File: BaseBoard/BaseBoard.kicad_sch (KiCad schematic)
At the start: 29 parts, among them J1 IMU, J2 Conn_01x04, J3 Raspberry_Pi_2_3, J4 USB_C_Receptacle_USB2.0, J5 Conn_02x04, SW1 SW_Push, SW2 SW_Push, U1 GD32VF103Cx, Y1 8Mhz

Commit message: 使用功率地
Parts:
- removed U1: GD32VF103Cx, Package_QFP:LQFP-48_7x7mm_P0.5mm, symbol GD32VF103:GD32VF103Cx
- added JP1: SolderJumper_2_Bridged, Jumper:SolderJumper-2_P1.3mm_Bridged2Bar_Pad1.0x1.5mm, symbol Jumper:SolderJumper_2_Bridged
- added U1: GD32VF103C8Tx, Package_QFP:LQFP-48_7x7mm_P0.5mm, symbol MCU_ST_STM32F1:STM32F103C8Tx
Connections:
- net +3V3: now also SW1.1, U1.1 (VBAT), U1.24 (VDD), U1.36 (VDD), U1.48 (VDD), U1.9 (VDDA); no longer SW1.2
- net ADC: now also U1.18 (PB0)
- net BOOT0: now also SW1.2, U1.44 (BOOT0); no longer SW1.1
- net BOOT1: now also U1.20 (PB2)
- net CTL_RX: now also U1.13 (PA3)
- net CTL_TX: now also U1.12 (PA2)
- net DEBUG_RX: now also U1.22 (PB11)
- net DEBUG_TX: now also U1.21 (PB10)
- net ENC1_A: now also U1.40 (PB4)
- net ENC1_B: now also U1.41 (PB5)
- net ENC2_A: now also U1.42 (PB6)
- net ENC2_B: now also U1.43 (PB7)
- net ENC3_A: now also U1.10 (PA0)
- net ENC3_B: now also U1.11 (PA1)
- net GND: now also JP1.1 (A), U1.23 (VSS), U1.35 (VSS), U1.47 (VSS), U1.8 (VSSA)
- net JTCK: now also U1.37 (PA14)
- net JTDI: now also U1.38 (PA15)
- net JTDO: now also U1.39 (PB3)
- net JTMS: now also U1.34 (PA13)
- net OSC32_IN: now also U1.3 (PC14)
- net OSC32_OUT: now also U1.4 (PC15)
- net OSCIN: now also U1.5 (PD0)
- net OSCOUT: now also U1.6 (PD1)
- net PWM1: now also U1.29 (PA8)
- net PWM1_ON: now also U1.26 (PB13)
- net PWM2: now also U1.30 (PA9)
- net PWM2_ON: now also U1.27 (PB14)
- net PWM3: now also U1.31 (PA10)
- net PWM3_ON: now also U1.28 (PB15)
- net USB_DM: now also U1.32 (PA11)
- net USB_DP: now also U1.33 (PA12)
- net at D1.1 (K): now also U1.2 (PC13)
- net at C8.1, R7.1, SW2.2: now also U1.7 (NRST)
- new net GNDPWR: JP1.2 (B)
- no-connect marks 6 -> 2
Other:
- moved on the sheet: C8, D1, R7, R8, SW2

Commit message: 临时提交
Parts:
- added J13: Conn_01x02_Female, Connector_JST:JST_PH_S2B-PH-K_1x02_P2.00mm_Horizontal, symbol Connector:Conn_01x02_Female
- added J14: Conn_01x03_Female, Connector_JST:JST_PH_S3B-PH-K_1x03_P2.00mm_Horizontal, symbol Connector:Conn_01x03_Female
- added R11: 10k, Resistor_SMD:R_0805_2012Metric, symbol Device:R_Small
- J2: footprint Connector_JST:JST_XH_B4B-XH-A_1x04_P2.50mm_Vertical -> Connector_JST:JST_PH_S4B-PH-K_1x04_P2.00mm_Horizontal
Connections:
- net +3V3: now also SW1.2, R11.1; no longer SW1.1
- net BOOT0: now also SW1.1; no longer SW1.2
- net GND: now also SW2.2, J13.2 (Pin_2); no longer SW2.1
- net GNDPWR: now also J14.3 (Pin_3)
- net at C8.1, R7.1, U1.7 (NRST): now also SW2.1; no longer SW2.2
- net BREAK: now reaches U1.25 (PB12)
- net BREAK: now also J13.1 (Pin_1), R11.2
- net USB_DM renamed PWM4
- net PWM4: now also J14.2 (Pin_2)
- new net +12VA: J14.1 (Pin_1)
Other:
- moved on the sheet: J5

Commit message: 更新V3线路板
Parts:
- removed J1: IMU, Connector_PinSocket_2.54mm:PinSocket_1x10_P2.54mm_Vertical, symbol Connector_Generic:Conn_01x10
- added U7: BMI088, Smallbot:Bochs_LGA16_2x7+2x1, symbol Smallbot:BMI088
- J14: value Conn_01x03_Female -> PH2.0_1x03
- J2: value Conn_01x04 -> PH2.0_1x04
- J5: value Conn_02x04 -> PinHeader_2.54_1x04
- JP1: value SolderJumper_2_Bridged -> NC
- SW1, SW2: value SW_Push -> TL3342; footprint User_Button_Switch:SW_SPST_EVQP7C-Single -> Button_Switch_SMD:SW_SPST_TL3342
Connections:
- net +12VA: now also J14.3 (Pin_3); no longer J14.1 (Pin_1)
- net +3.3VA: now also U7.11 (VDDIO), U7.3 (VDD)
- net GND: now also J14.1 (Pin_1), U7.2 (NC), U7.4 (GNDA), U7.6 (GNDIO), U7.7 (PS)
- net GNDPWR: no longer J14.3 (Pin_3)
- net LIDAR_RX: now also J3.7 (GCLK0/GPIO4); no longer J3.24 (~{CE0}/GPIO8)
- net LIDAR_TX: now also J3.29 (GCLK1/GPIO5); no longer J3.21 (MISO0/GPIO9)
- net SPI_CS2: now reaches J3.26 (~{CE1}/GPIO7)
- net SPI_CS2: now also U7.5 (CSB2)
- net I2C_SCL: now reaches U1.45 (PB8)
- net I2C_SDA: now reaches U1.46 (PB9)
- net GPIO10 renamed SPI_MOSI
- net SPI_MOSI: now also U7.9 (SDA/MOSI)
- net GPIO11 renamed SPI_CLK
- net SPI_CLK: now also U7.8 (SCL/CLK)
- net GPIO22: no longer names the net of J3.15 (GPIO22)
- net GPIO23: no longer names the net of J3.16 (GPIO23)
- net GPIO24 renamed IMU_INT2
- net IMU_INT2: now also U7.12 (INT3)
- net GPIO25 renamed IMU_INT1
- net IMU_INT1: now also U7.16 (INT1)
- net SCL: no longer names the net of J3.5 (SCL/GPIO3)
- net SDA: no longer names the net of J3.3 (SDA/GPIO2)
- new net SPI_CS1: J3.24 (~{CE0}/GPIO8), U7.14 (CSB1)
- new net SPI_MISO: J3.21 (MISO0/GPIO9), U7.10 (MISO2), U7.15 (MISO1)
- no-connect marks 2 -> 4
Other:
- sheet Power ports: added SCL, SDA; removed none
- note removed: "VCC GND SCL SDA UNO0 UNO1 UNO2 UNO3 UNO4 UNO5"
- moved on the sheet: J2

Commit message: 添加v3初版设计
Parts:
- renumbered J2 to J1, J3 to J2, J4 to J3, J5 to J4, J13 to J5, J14 to J6, R8 to R7, R7 to R8, R11 to R9, U7 to U1, U1 to U2

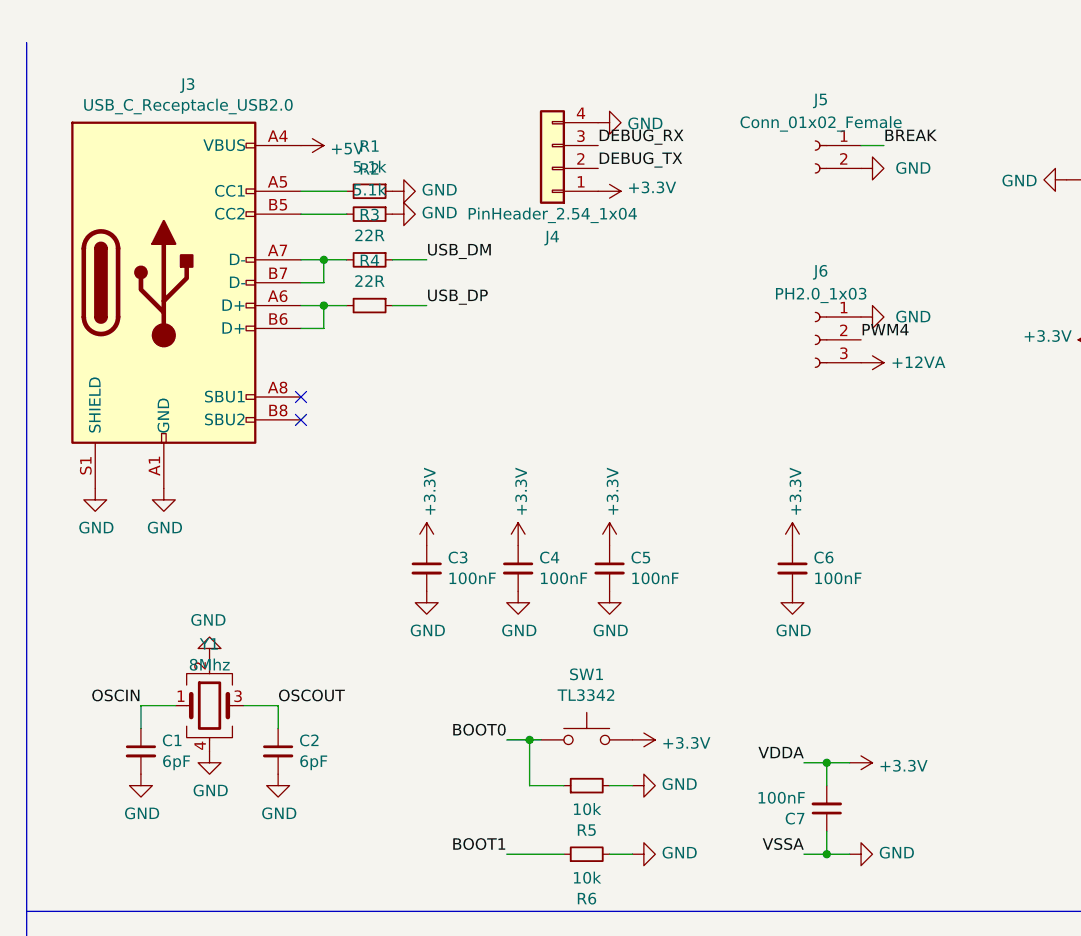
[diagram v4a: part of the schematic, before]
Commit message: 修改部分封装和值
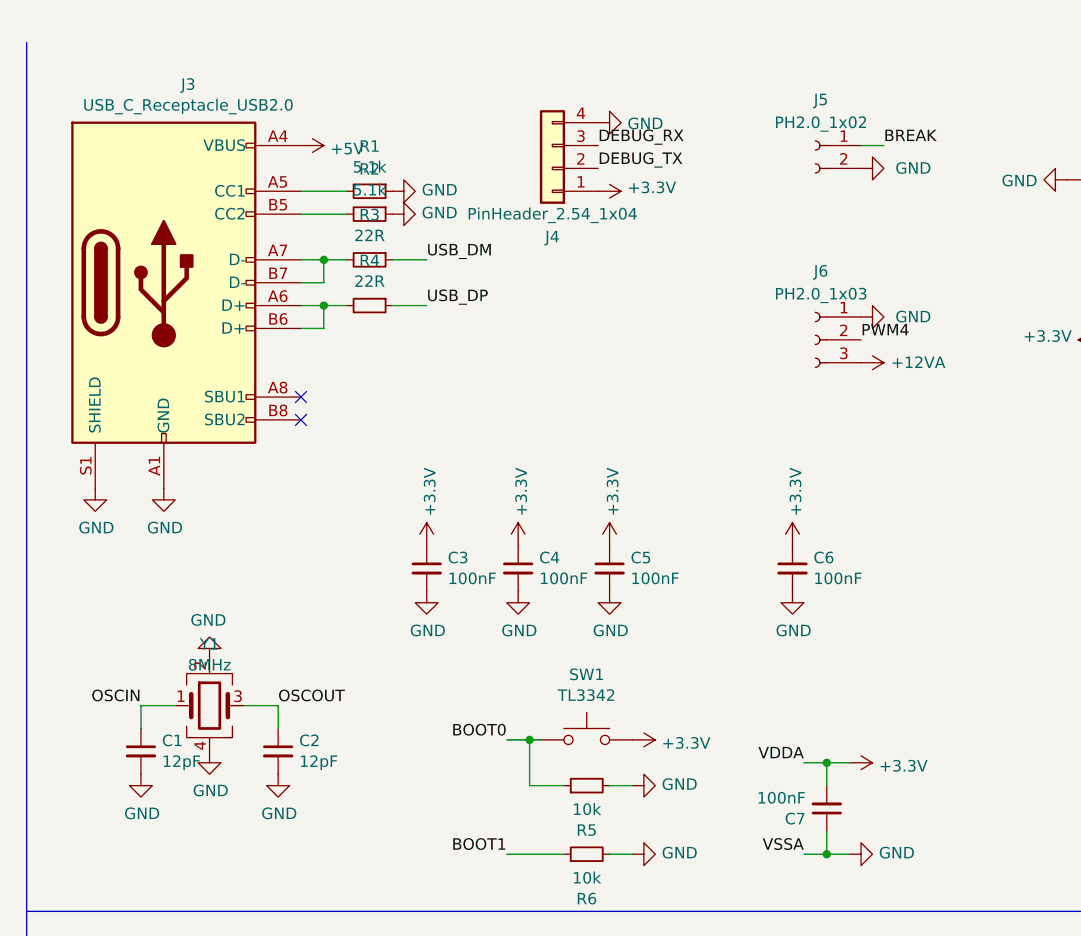
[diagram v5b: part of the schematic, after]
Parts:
- C1, C2: value 6pF -> 12pF
- J5: value Conn_01x02_Female -> PH2.0_1x02
- Y1: value 8Mhz -> 8MHz
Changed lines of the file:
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@@
       (effects (font (size 1.27 1.27)))
     )
-    (property "Value" "8Mhz" (at 113.03 83.1342 0)
+    (property "Value" "8MHz" (at 113.03 83.1342 0)
       (effects (font (size 1.27 1.27)))
     )
@@
       (effects (font (size 1.27 1.27)) (justify left))
     )
-    (property "Value" "6pF" (at 107.7468 93.853 0)
+    (property "Value" "12pF" (at 107.7468 93.853 0)
       (effects (font (size 1.27 1.27)) (justify left))
     )
@@
       (effects (font (size 1.27 1.27)) (justify left))
     )
-    (property "Value" "6pF" (at 122.9868 93.853 0)
+    (property "Value" "12pF" (at 122.9868 93.853 0)
       (effects (font (size 1.27 1.27)) (justify left))
     )
@@
       (effects (font (size 1.27 1.27)))
     )
-    (property "Value" "Conn_01x02_Female" (at 180.975 22.86 0)
-      (effects (font (size 1.27 1.27)))
-    )
+    (property "Value" "PH2.0_1x02" (at 180.975 22.86 0)
+      (effects (font (size 1.27 1.27)))
+    )
